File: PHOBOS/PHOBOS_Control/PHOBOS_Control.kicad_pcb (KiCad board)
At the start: 2 copper layers, 1 x 0.6 mm, 80 parts, among them J1 Screw_Terminal_01x02, J3 Conn_Coaxial, J4 Conn_01x03, J5 Conn_01x03, J6 USB4056-03-A_REVA2, U1 SX1280IMLTRT, U2 TLV9351IDCKR, U3 W25Q128JVSIQ, U4 NCP1117-3.3_SOT223, U5 RP2040, U6 TLV9351IDCKR, U7 TLV9351IDCKR, U8 TLV9351IDCKR, Y1 ABM8-272-T3, Y2 C1E-52.000-10-1012-X-M

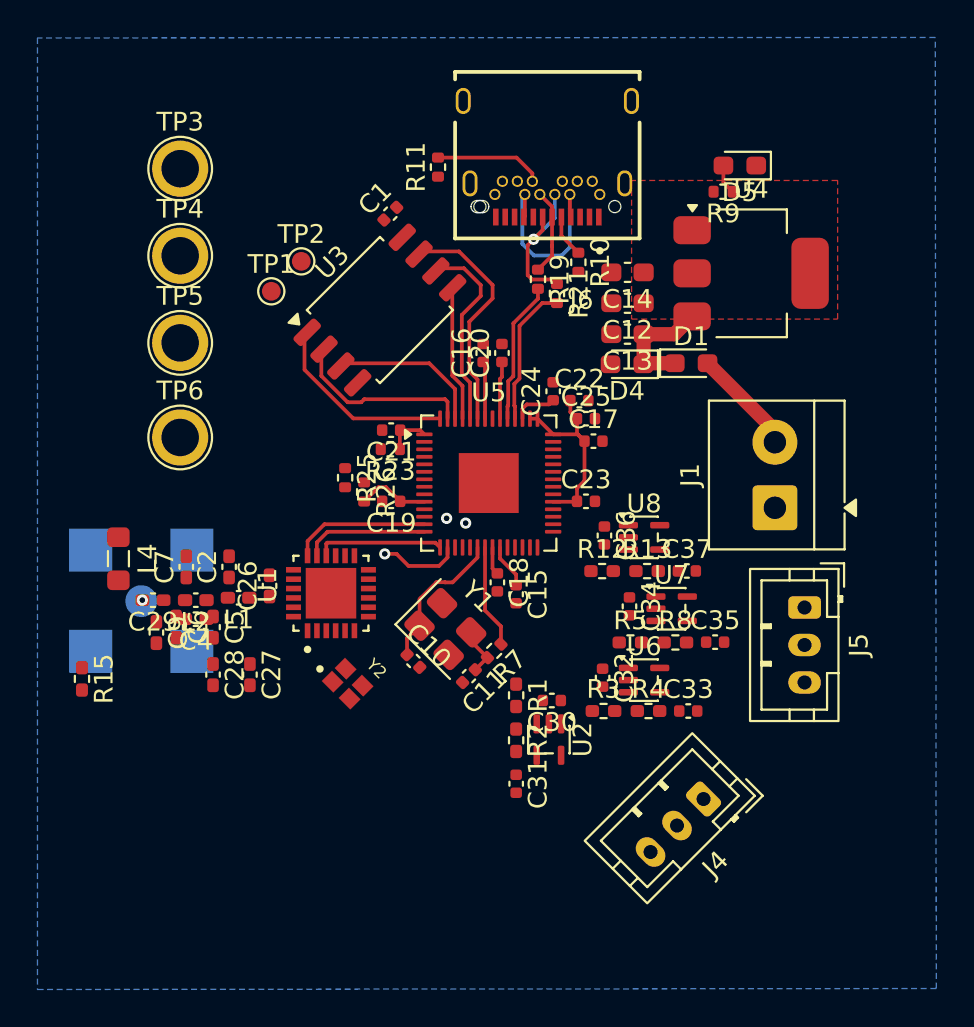
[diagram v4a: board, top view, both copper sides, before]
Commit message: mounting holes added and shape changed. design blocks utilized
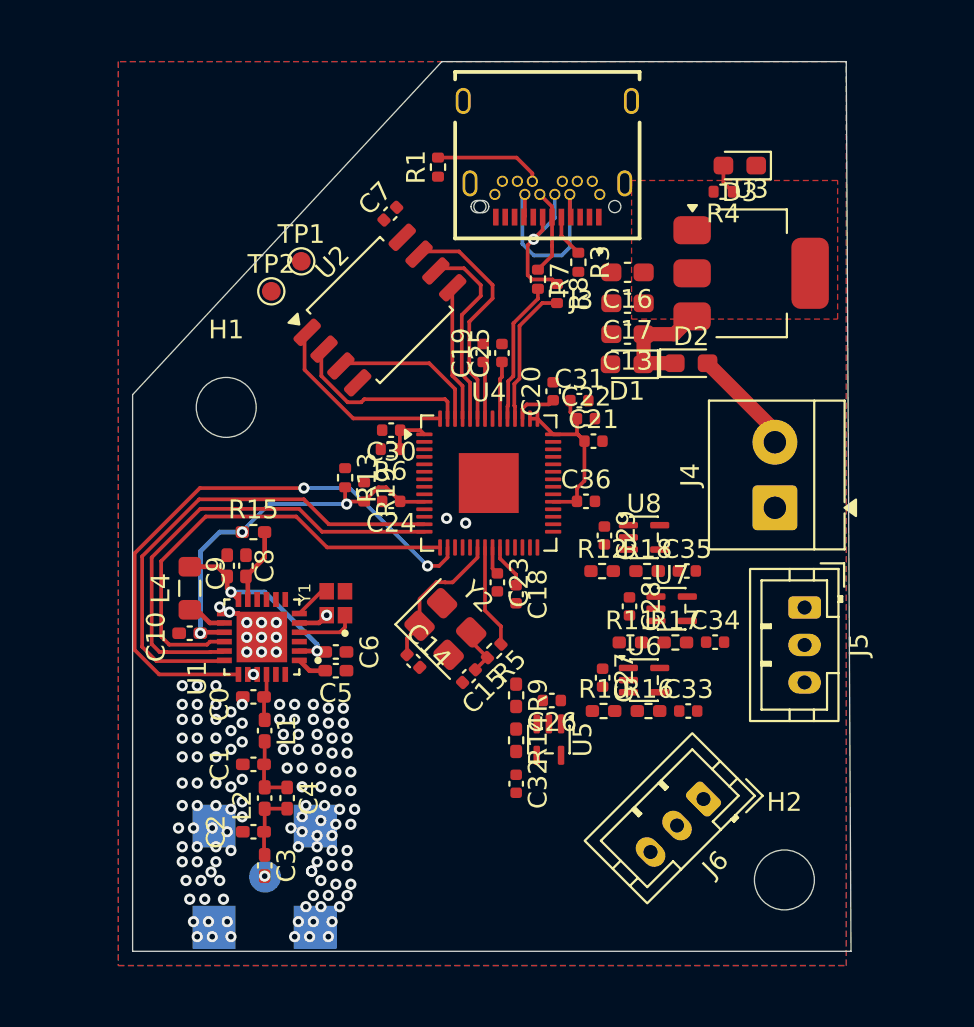
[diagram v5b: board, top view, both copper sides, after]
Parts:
- removed the C26 at (78.4, 433.1)
- removed the C27 at (77.4, 437.9)
- removed the C28 at (75.4, 437.9)
- removed the C29 at (72.2, 433.9)
- removed the C7 at (74.0, 432.1)
- removed the J3 at (71.6, 433.9)
- removed TP3: SCK, TestPoint:TestPoint_Plated_Hole_D2.0mm
- removed TP4: MOSI, TestPoint:TestPoint_Plated_Hole_D2.0mm
- removed TP5: MISO, TestPoint:TestPoint_Plated_Hole_D2.0mm
- removed TP6: CS, TestPoint:TestPoint_Plated_Hole_D2.0mm
- removed the Y2 at (82.6, 438.3)
- added C0: .8P, Capacitor_SMD:C_0402_1005Metric_Pad0.74x0.62mm_HandSolder, F.Cu at (77.6, 439.0)
- added C1: 1.2p, Capacitor_SMD:C_0402_1005Metric_Pad0.74x0.62mm_HandSolder, F.Cu at (77.6, 442.6)
- added C10: 100n, Capacitor_SMD:C_0402_1005Metric_Pad0.74x0.62mm_HandSolder, F.Cu at (74.2, 435.6)
- added C3: 100p, Capacitor_SMD:C_0402_1005Metric_Pad0.74x0.62mm_HandSolder, F.Cu at (78.2, 448.0)
- added C8: 100n, Capacitor_SMD:C_0402_1005Metric_Pad0.74x0.62mm_HandSolder, F.Cu at (77.2, 432.0)
- added H1: MountingHole, MountingHole:MountingHole_3.2mm_M3, F.Cu at (76.1, 423.6)
- added H2: MountingHole, MountingHole:MountingHole_3.2mm_M3, F.Cu at (105.9, 448.8)
- added J2: Conn_Coaxial, SMA_J_P_GF_RA_SM1:SAMTEC_SMA-J-P-GF-RA-SM1, B.Cu at (78.2, 448.6)
- added Y1: C1E-52.000-10-1012-X-M, C1E-52.000-10-1012-X-M:XTAL_C1E-52.000-10-1012-X-M, F.Cu at (82.0, 434.0)
- moved C2 14.2 mm to (77.6, 446.2), turned to 180 degrees
- moved R15 12.0 mm to (77.6, 430.2), turned to 180 degrees
- moved L2 11.2 mm to (78.2, 444.4), turned to -90 degrees
- moved C4 10.7 mm to (79.4, 444.4), turned to -90 degrees
- moved C6 8.63 mm to (82.0, 436.6), turned to 0 degrees
- moved L1 7.23 mm to (78.2, 440.8), turned to -90 degrees
- moved C5 6.96 mm to (82.0, 437.6), turned to 0 degrees
- moved C9 5.19 mm to (76.2, 432.0), turned to 90 degrees
- moved U1 4.37 mm to (78.0, 435.8), turned to 180 degrees
- moved L4 4.12 mm to (74.2, 433.2), turned to 90 degrees
- renumbered C10 to C14, C11 to C15, C14 to C16, C12 to C17, C15 to C18, C16 to C19, C24 to C20, C17 to C21, C25 to C22, C18 to C23, C19 to C24, C20 to C25, C30 to C26, C32 to C27, C34 to C28, C36 to C29, C21 to C30, C22 to C31, C31 to C32, C35 to C34, C37 to C35, C23 to C36, C1 to C7, D4 to D1, D1 to D2, D5 to D3, J6 to J3, J1 to J4, J4 to J6, R11 to R1, R3 to R10, R5 to R11, R25 to R13, R2 to R14, R4 to R16, R8 to R17, R13 to R18, R26 to R19, R10 to R3, R9 to R4, R7 to R5, R23 to R6, R19 to R7, R21 to R8, R1 to R9, TP2 to TP1, TP1 to TP2, U3 to U2, U4 to U3, U5 to U4, U2 to U5, Y1 to Y2
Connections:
- C4 pad 1: Net-(C2-Pad1) -> Net-(C1-Pad1)
- C4 pad 2: Net-(C29-Pad1) -> Net-(C2-Pad1)
- L1 pad 2: Net-(C2-Pad1) -> Net-(C1-Pad1)
- L2 pad 1: Net-(C2-Pad1) -> Net-(C1-Pad1)
- L2 pad 2: Net-(C29-Pad1) -> Net-(C2-Pad1)
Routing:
- net /NSS: track 4.34 -> 31.8 mm, vias 1 -> 2
- net /SCK: track 7.39 -> 26.4 mm
- net /MOSI: track 6.69 -> 24.8 mm
- net /MISO: track 6.85 -> 24.2 mm
- net +3V3: track 21.4 -> 37.9 mm, vias 0 -> 3
- net /DCC_FB: track 0.00 -> 11.2 mm, vias 0 -> 2
- net GND: track 0.00 -> 4.15 mm, vias 0 -> 134
- net /VBAT_IO: track 0.00 -> 4.05 mm
- net Net-(C2-Pad1): track 0.00 -> 3.69 mm
- net Net-(C1-Pad1): track 0.00 -> 3.68 mm
- net /XTA: track 0.00 -> 3.19 mm
- net /RFIO: track 0.00 -> 2.50 mm
- net /DCC_SW: track 0.00 -> 2.14 mm
- net /XTB: track 0.00 -> 1.95 mm
- net /VR_PA: track 0.00 -> 1.61 mm
- added copper zone on F.Cu, net GND
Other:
- board size 1 x 0.6 mm -> 38.4 x 47.5 mm

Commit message: PCB routed. perhaps add thermal reliefs on GND plane.
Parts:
- removed J5, J6: Conn_01x03, Connector_JST:JST_PH_B3B-PH-K_1x03_P2.00mm_Vertical
- removed TP1: GND, TestPoint:TestPoint_Pad_D1.0mm
- removed TP2: Boot, TestPoint:TestPoint_Pad_D1.0mm
- added J7: Conn_01x05, Connector_JST:JST_PH_B5B-PH-K_1x05_P2.00mm_Vertical, F.Cu at (172.4, 105.3)
- added J8: Conn_01x02, Connector_PinHeader_2.54mm:PinHeader_1x02_P2.54mm_Vertical, F.Cu at (144.5, 88.4)
- moved H1 349.2 mm to (147.7, 81.8)
- moved C32 337.2 mm to (168.1, 115.3), turned to 0 degrees
- moved R5 337.1 mm to (160.1, 106.7), turned to -45 degrees
- moved D1 336.8 mm to (163.2, 91.0), turned to 90 degrees
- moved C15 336.8 mm to (160.2, 108.8)
- moved C17 336.7 mm to (165.0, 88.2), turned to 90 degrees
- moved C18 336.1 mm to (159.7, 104.4), turned to -45 degrees
- moved J4 336.1 mm to (170.8, 99.3)
- moved D2 336.1 mm to (169.6, 92.2)
- moved U5 335.6 mm to (165.8, 113.6), turned to 0 degrees
- moved C29 335.6 mm to (163.1, 101.5)
- moved C35 335.6 mm to (167.5, 103.4)
- moved R12 335.6 mm to (163.0, 103.4)
- moved R18 335.6 mm to (165.4, 103.4)
- moved U8 335.6 mm to (165.3, 101.6)
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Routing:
- net +3V3: track 37.9 -> 102.3 mm, vias 3 -> 8
- net +BATT: track 5.71 -> 30.4 mm, vias 0 -> 4
- net +1V1: track 7.80 -> 22.3 mm, vias 0 -> 3
- net /PS4MCU: track 0.00 -> 13.5 mm
- net /PS3MCU: track 0.00 -> 9.77 mm
- net /PS4: track 0.00 -> 8.72 mm
- net /PS1: track 0.00 -> 8.29 mm
- net /PS2: track 0.00 -> 7.87 mm
- net /PS3: track 0.00 -> 7.75 mm
- net /QSPI_SS: track 10.4 -> 17.6 mm
- net GND: track 4.15 -> 10.5 mm, vias 134 -> 168
- net /PS2MCU: track 0.00 -> 6.30 mm
- net VBUS: track 11.0 -> 16.6 mm
- net /SDA: track 0.00 -> 4.33 mm
- net /PS1MCU: track 0.00 -> 3.67 mm
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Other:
- board size 38.4 x 47.5 mm -> 34.7 x 49.9 mm
- board text added: "Kyle Eckert"
- board text added: "P.H.O.B.O.S. Control"
